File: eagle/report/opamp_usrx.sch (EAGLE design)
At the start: 11 parts, among them IC1 LM324N

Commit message: Continued design and implementation.
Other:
- moved on the sheet: R7
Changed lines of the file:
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@@
 <?xml version="1.0" encoding="utf-8"?>
 <!DOCTYPE eagle SYSTEM "eagle.dtd">
-<eagle version="6.3">
+<eagle version="6.4">
 <drawing>
 <settings>
@@
 <instance part="R3" gate="G$1" x="185.42" y="203.2"/>
 <instance part="R2" gate="1" x="160.02" y="215.9" rot="R270"/>
-<instance part="R7" gate="1" x="231.14" y="208.28" rot="R180"/>
+<instance part="R7" gate="1" x="241.3" y="208.28" rot="R180"/>
 <instance part="R4" gate="1" x="200.66" y="213.36" rot="R270"/>
 <instance part="C1" gate="G$1" x="132.08" y="205.74" rot="R90"/>
@@
 <instance part="C3" gate="G$1" x="172.72" y="203.2" rot="R90"/>
 <instance part="C4" gate="G$1" x="200.66" y="223.52" rot="R90"/>
-<instance part="IC1" gate="P" x="243.84" y="208.28"/>
-<instance part="GND2" gate="1" x="243.84" y="195.58"/>
+<instance part="IC1" gate="P" x="254" y="208.28"/>
+<instance part="GND2" gate="1" x="254" y="195.58"/>
 <instance part="U$2" gate="G$1" x="124.46" y="200.66" rot="R90"/>
 <instance part="GND7" gate="1" x="127" y="193.04"/>
-<instance part="P+1" gate="VCC" x="243.84" y="220.98"/>
+<instance part="P+1" gate="VCC" x="254" y="220.98"/>
 </instances>
 <busses>
@@
 <segment>
 <pinref part="R7" gate="1" pin="S"/>
-<wire x1="226.06" y1="208.28" x2="223.52" y2="208.28" width="0.1524" layer="91"/>
-<label x="223.52" y="208.28" size="1.778" layer="95" rot="R270"/>
+<wire x1="236.22" y1="208.28" x2="233.68" y2="208.28" width="0.1524" layer="91"/>
+<label x="233.68" y="208.28" size="1.778" layer="95" rot="R270"/>
 </segment>
 </net>
@@
 <segment>
 <pinref part="IC1" gate="P" pin="V-"/>
-<wire x1="243.84" y1="200.66" x2="231.14" y2="200.66" width="0.1524" layer="91"/>
+<wire x1="254" y1="200.66" x2="241.3" y2="200.66" width="0.1524" layer="91"/>
 <pinref part="R7" gate="1" pin="E"/>
-<wire x1="231.14" y1="200.66" x2="231.14" y2="203.2" width="0.1524" layer="91"/>
-<wire x1="243.84" y1="200.66" x2="243.84" y2="198.12" width="0.1524" layer="91"/>
-<junction x="243.84" y="200.66"/>
+<wire x1="241.3" y1="200.66" x2="241.3" y2="203.2" width="0.1524" layer="91"/>
+<wire x1="254" y1="200.66" x2="254" y2="198.12" width="0.1524" layer="91"/>
+<junction x="254" y="200.66"/>
 <pinref part="GND2" gate="1" pin="GND"/>
 </segment>
@@
 <pinref part="IC1" gate="P" pin="V+"/>
 <pinref part="P+1" gate="VCC" pin="VCC"/>
-<wire x1="243.84" y1="218.44" x2="243.84" y2="215.9" width="0.1524" layer="91"/>
+<wire x1="254" y1="218.44" x2="254" y2="215.9" width="0.1524" layer="91"/>
 <pinref part="R7" gate="1" pin="A"/>
-<wire x1="231.14" y1="215.9" x2="231.14" y2="213.36" width="0.1524" layer="91"/>
-<wire x1="231.14" y1="215.9" x2="243.84" y2="215.9" width="0.1524" layer="91"/>
-<junction x="243.84" y="215.9"/>
-</segment>
-</net>
+<wire x1="241.3" y1="215.9" x2="241.3" y2="213.36" width="0.1524" layer="91"/>
+<wire x1="241.3" y1="215.9" x2="254" y2="215.9" width="0.1524" layer="91"/>
+<junction x="254" y="215.9"/>
+</segment>
+</net>

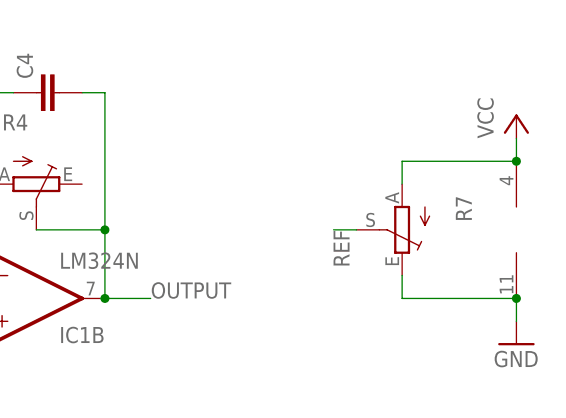
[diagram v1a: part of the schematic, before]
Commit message: Removed pot from blueboard schematic.
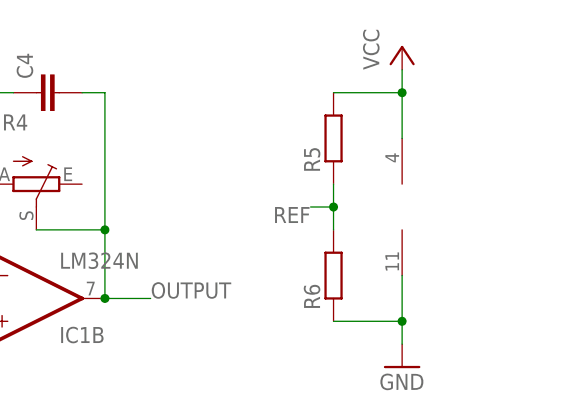
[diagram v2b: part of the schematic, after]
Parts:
- removed R7: (no value), pot:TRIM_EU-S63P
- added R5, R6: (no value), rcl:R-EU_0207/2V
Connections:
- net GND: now also R6.1; no longer R7.E
- net REF: now also R5.1, R6.2; no longer R7.S
- net VCC: now also R5.2; no longer R7.A
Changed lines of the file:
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@@
 <?xml version="1.0" encoding="utf-8"?>
 <!DOCTYPE eagle SYSTEM "eagle.dtd">
-<eagle version="6.4">
+<eagle version="6.3">
 <drawing>
 <settings>
@@
 <part name="R3" library="rcl" deviceset="R-EU_" device="0207/2V"/>
 <part name="R2" library="pot" deviceset="TRIM_EU-" device="S63P"/>
-<part name="R7" library="pot" deviceset="TRIM_EU-" device="S63P"/>
 <part name="R4" library="pot" deviceset="TRIM_EU-" device="S63P"/>
 <part name="C1" library="rcl" deviceset="C-EU" device="025-025X050"/>
@@
 <part name="GND7" library="supply1" deviceset="GND" device=""/>
 <part name="P+1" library="supply1" deviceset="VCC" device=""/>
+<part name="R5" library="rcl" deviceset="R-EU_" device="0207/2V"/>
+<part name="R6" library="rcl" deviceset="R-EU_" device="0207/2V"/>
 </parts>
 <sheets>
@@
 <instance part="R3" gate="G$1" x="185.42" y="203.2"/>
 <instance part="R2" gate="1" x="160.02" y="215.9" rot="R270"/>
-<instance part="R7" gate="1" x="241.3" y="208.28" rot="R180"/>
 <instance part="R4" gate="1" x="200.66" y="213.36" rot="R270"/>
 <instance part="C1" gate="G$1" x="132.08" y="205.74" rot="R90"/>
@@
 <instance part="C3" gate="G$1" x="172.72" y="203.2" rot="R90"/>
 <instance part="C4" gate="G$1" x="200.66" y="223.52" rot="R90"/>
-<instance part="IC1" gate="P" x="254" y="208.28"/>
-<instance part="GND2" gate="1" x="254" y="195.58"/>
+<instance part="IC1" gate="P" x="241.3" y="210.82"/>
+<instance part="GND2" gate="1" x="241.3" y="193.04"/>
 <instance part="U$2" gate="G$1" x="124.46" y="200.66" rot="R90"/>
 <instance part="GND7" gate="1" x="127" y="193.04"/>
-<instance part="P+1" gate="VCC" x="254" y="220.98"/>
+<instance part="P+1" gate="VCC" x="241.3" y="228.6"/>
+<instance part="R5" gate="G$1" x="233.68" y="218.44" rot="R90"/>
+<instance part="R6" gate="G$1" x="233.68" y="203.2" rot="R90"/>
 </instances>
 <busses>
@@
 </segment>
 <segment>
-<pinref part="R7" gate="1" pin="S"/>
-<wire x1="236.22" y1="208.28" x2="233.68" y2="208.28" width="0.1524" layer="91"/>
-<label x="233.68" y="208.28" size="1.778" layer="95" rot="R270"/>
+<label x="231.14" y="210.82" size="1.778" layer="95" rot="R180"/>
+<pinref part="R5" gate="G$1" pin="1"/>
+<pinref part="R6" gate="G$1" pin="2"/>
+<wire x1="233.68" y1="213.36" x2="233.68" y2="210.82" width="0.1524" layer="91"/>
+<wire x1="233.68" y1="210.82" x2="233.68" y2="208.28" width="0.1524" layer="91"/>
+<wire x1="233.68" y1="210.82" x2="231.14" y2="210.82" width="0.1524" layer="91"/>
+<junction x="233.68" y="210.82"/>
 </segment>
 </net>
@@
 <segment>
 <pinref part="IC1" gate="P" pin="V-"/>
-<wire x1="254" y1="200.66" x2="241.3" y2="200.66" width="0.1524" layer="91"/>
-<pinref part="R7" gate="1" pin="E"/>
-<wire x1="241.3" y1="200.66" x2="241.3" y2="203.2" width="0.1524" layer="91"/>
-<wire x1="254" y1="200.66" x2="254" y2="198.12" width="0.1524" layer="91"/>
-<junction x="254" y="200.66"/>
+<wire x1="241.3" y1="203.2" x2="241.3" y2="198.12" width="0.1524" layer="91"/>
 <pinref part="GND2" gate="1" pin="GND"/>
+<pinref part="R6" gate="G$1" pin="1"/>
+<wire x1="241.3" y1="198.12" x2="241.3" y2="195.58" width="0.1524" layer="91"/>
+<wire x1="233.68" y1="198.12" x2="241.3" y2="198.12" width="0.1524" layer="91"/>
+<junction x="241.3" y="198.12"/>
 </segment>
 <segment>
@@
 <pinref part="IC1" gate="P" pin="V+"/>
 <pinref part="P+1" gate="VCC" pin="VCC"/>
-<wire x1="254" y1="218.44" x2="254" y2="215.9" width="0.1524" layer="91"/>
-<pinref part="R7" gate="1" pin="A"/>
-<wire x1="241.3" y1="215.9" x2="241.3" y2="213.36" width="0.1524" layer="91"/>
-<wire x1="241.3" y1="215.9" x2="254" y2="215.9" width="0.1524" layer="91"/>
-<junction x="254" y="215.9"/>
-</segment>
-</net>
+<wire x1="241.3" y1="226.06" x2="241.3" y2="223.52" width="0.1524" layer="91"/>
+<pinref part="R5" gate="G$1" pin="2"/>
+<wire x1="241.3" y1="223.52" x2="241.3" y2="218.44" width="0.1524" layer="91"/>
+<wire x1="233.68" y1="223.52" x2="241.3" y2="223.52" width="0.1524" layer="91"/>
+<junction x="241.3" y="223.52"/>
+</segment>
+</net>
